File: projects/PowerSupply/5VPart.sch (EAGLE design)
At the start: 26 parts, among them IC1 LM2596T, IC2 LM2596T, X1 IN, X2 OUT

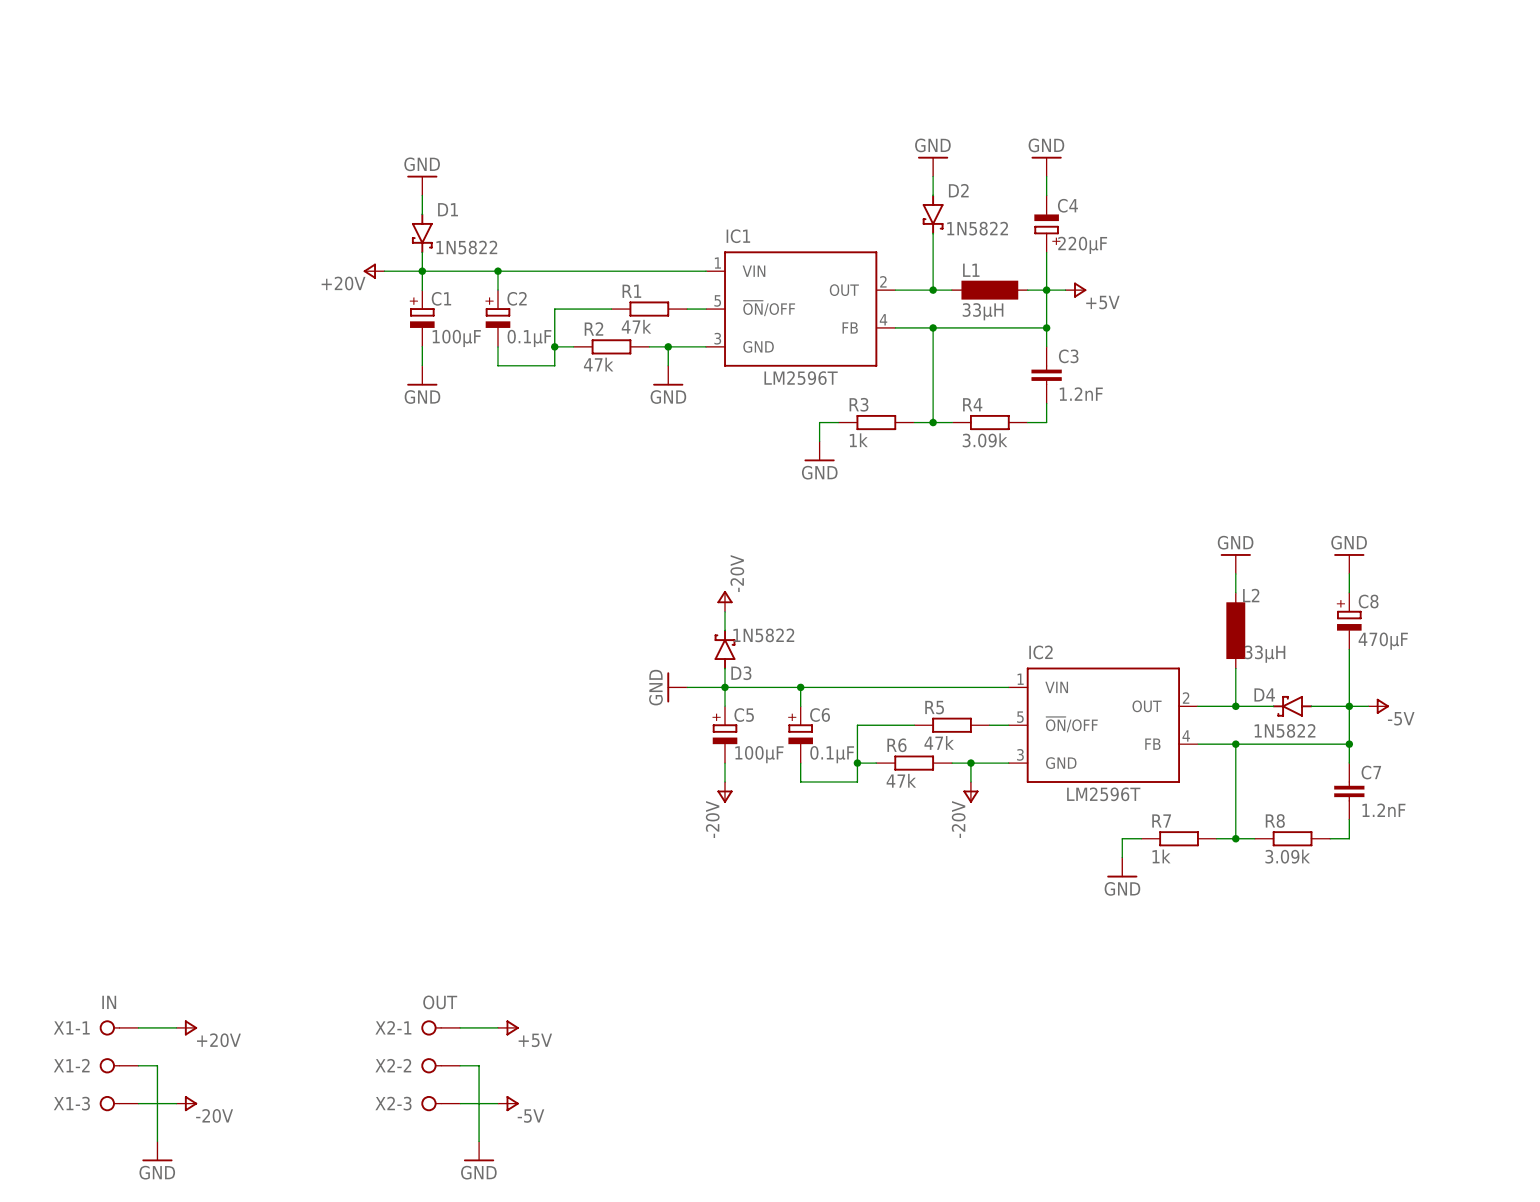
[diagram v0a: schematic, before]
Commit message: feat: 5 volt part modified
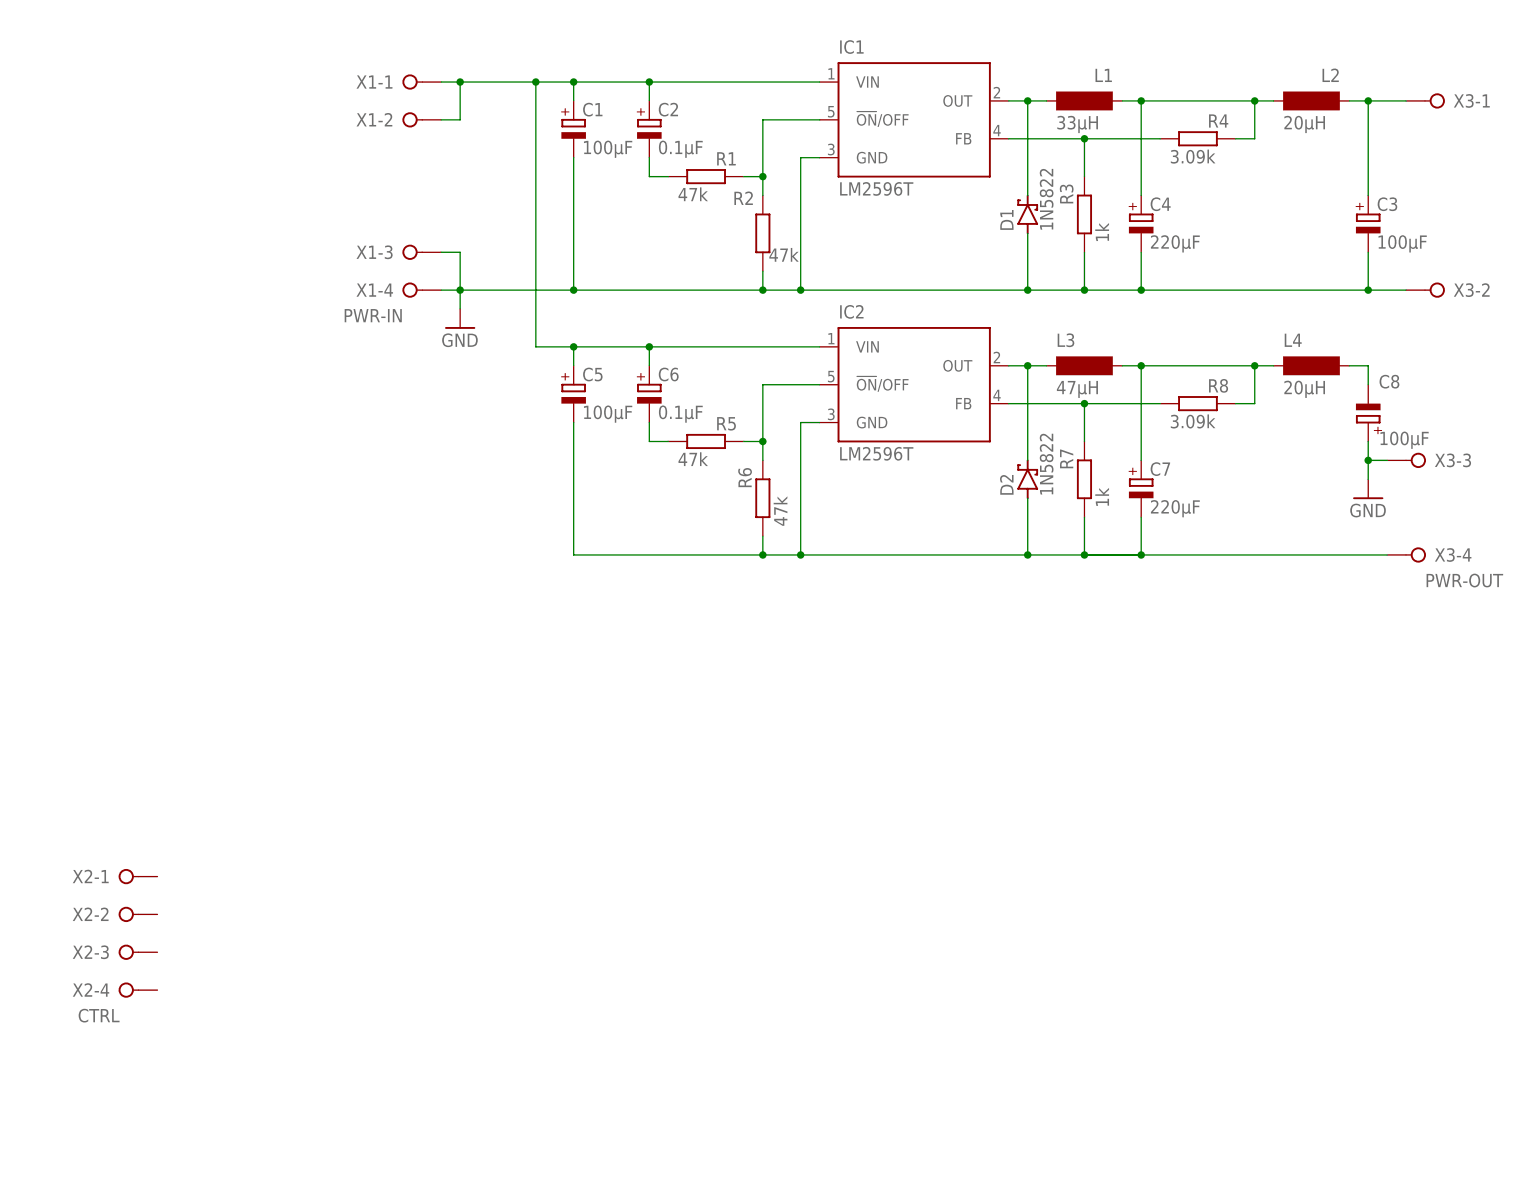
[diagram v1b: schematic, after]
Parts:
- removed D3, D4: 1N5822, diode:SCHOTTKY-DIODEC4111-15
- added L3: 47µH, bb84:IND-120-470K
- added L4: 20µH, bb84:B82111B0000C020
- added X3: PWR-OUT, con-wago-508:W237-04P
- C1, C5: device rcl:CPOL-EUE2.5-6 -> rcl:CPOL-EUE2.5-5
- C2, C6: device rcl:CPOL-EUE1.8-4 -> rcl:CPOL-EUE2-4
- C3: value 1.2nF -> 100µF; device rcl:C-EU050-024X044 -> rcl:CPOL-EUE2.5-5
- C7: value 1.2nF -> 220µF; device rcl:C-EU050-024X044 -> rcl:CPOL-EUE3.5-8
- C8: value 470µF -> 100µF; device rcl:CPOL-EUE3.5-8 -> rcl:CPOL-EUE2.5-5
- D1, D2: device diode:SCHOTTKY-DIODEC4111-15 -> diode:1N5908
- L2: value 33µH -> 20µH; device bb84:IND-120-330K -> bb84:B82111B0000C020
- X1: value IN -> PWR-IN; device con-wago-508:W237-03P -> con-wago-508:W237-04P
- X2: value OUT -> CTRL; device con-wago-508:W237-03P -> con-wago-508:W237-04P
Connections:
- removed net +20V: C1.+, C2.+, D1.C, IC1.VIN, X1-1.KL
- removed net +5V: C3.1, C4.+, IC1.FB, L1.2, R3.2, R4.1, X2-1.KL
- removed net -20V: C5.-, D3.C, IC2.GND, R6.2, X1-3.KL
- removed net -5V: C7.1, C8.-, D4.A, IC2.FB, R7.2, R8.1, X2-3.KL
- removed net N$3: D2.C, IC1.OUT, L1.1
- new net N$10: IC2.!ON!/OFF, R5.2, R6.2
- new net N$11: C5.-, C7.-, D2.A, IC2.GND, R6.1, R7.1, X3-4.KL
- new net N$12: D2.C, IC2.OUT, L3.1
- new net N$13: C7.+, L3.2, L4.1, R8.2
- new net N$14: IC2.FB, R7.2, R8.1
- new net N$15: C8.-, L4.2
- new net N$9: C6.-, R5.1
- net GND: now also C3.-, R2.1, X1-3.KL, X1-4.KL, X3-2.KL, X3-3.KL; no longer C5.+, C6.+, D2.A, D3.A, IC2.VIN, L2.2, R2.2, R7.1, X1-2.KL, X2-2.KL
- net N$1: now also C1.+, C2.+, C5.+, C6.+, IC1.VIN, IC2.VIN, X1-1.KL, X1-2.KL; no longer C3.2, R4.2
- net N$2: now also IC1.!ON!/OFF, R1.2, R2.2; no longer D4.C, IC2.OUT, L2.1
- net N$4: now also D1.C, IC1.OUT, L1.1; no longer IC1.!ON!/OFF, R1.2
- net N$5: now also IC1.FB, R3.2, R4.1; no longer C7.2, R8.2
- net N$6: now also C4.+, L1.2, L2.1, R4.2; no longer C2.-, R1.1, R2.1
- net N$7: now also C3.+, L2.2, X3-1.KL; no longer IC2.!ON!/OFF, R5.2
- net N$8: now also C2.-, R1.1; no longer C6.-, R5.1, R6.1
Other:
- moved on the sheet: C1, C2, C4, C5, C6, C8, IC1, IC2, L1, L2, R1, R2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

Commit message: feat: 5 volt part modified
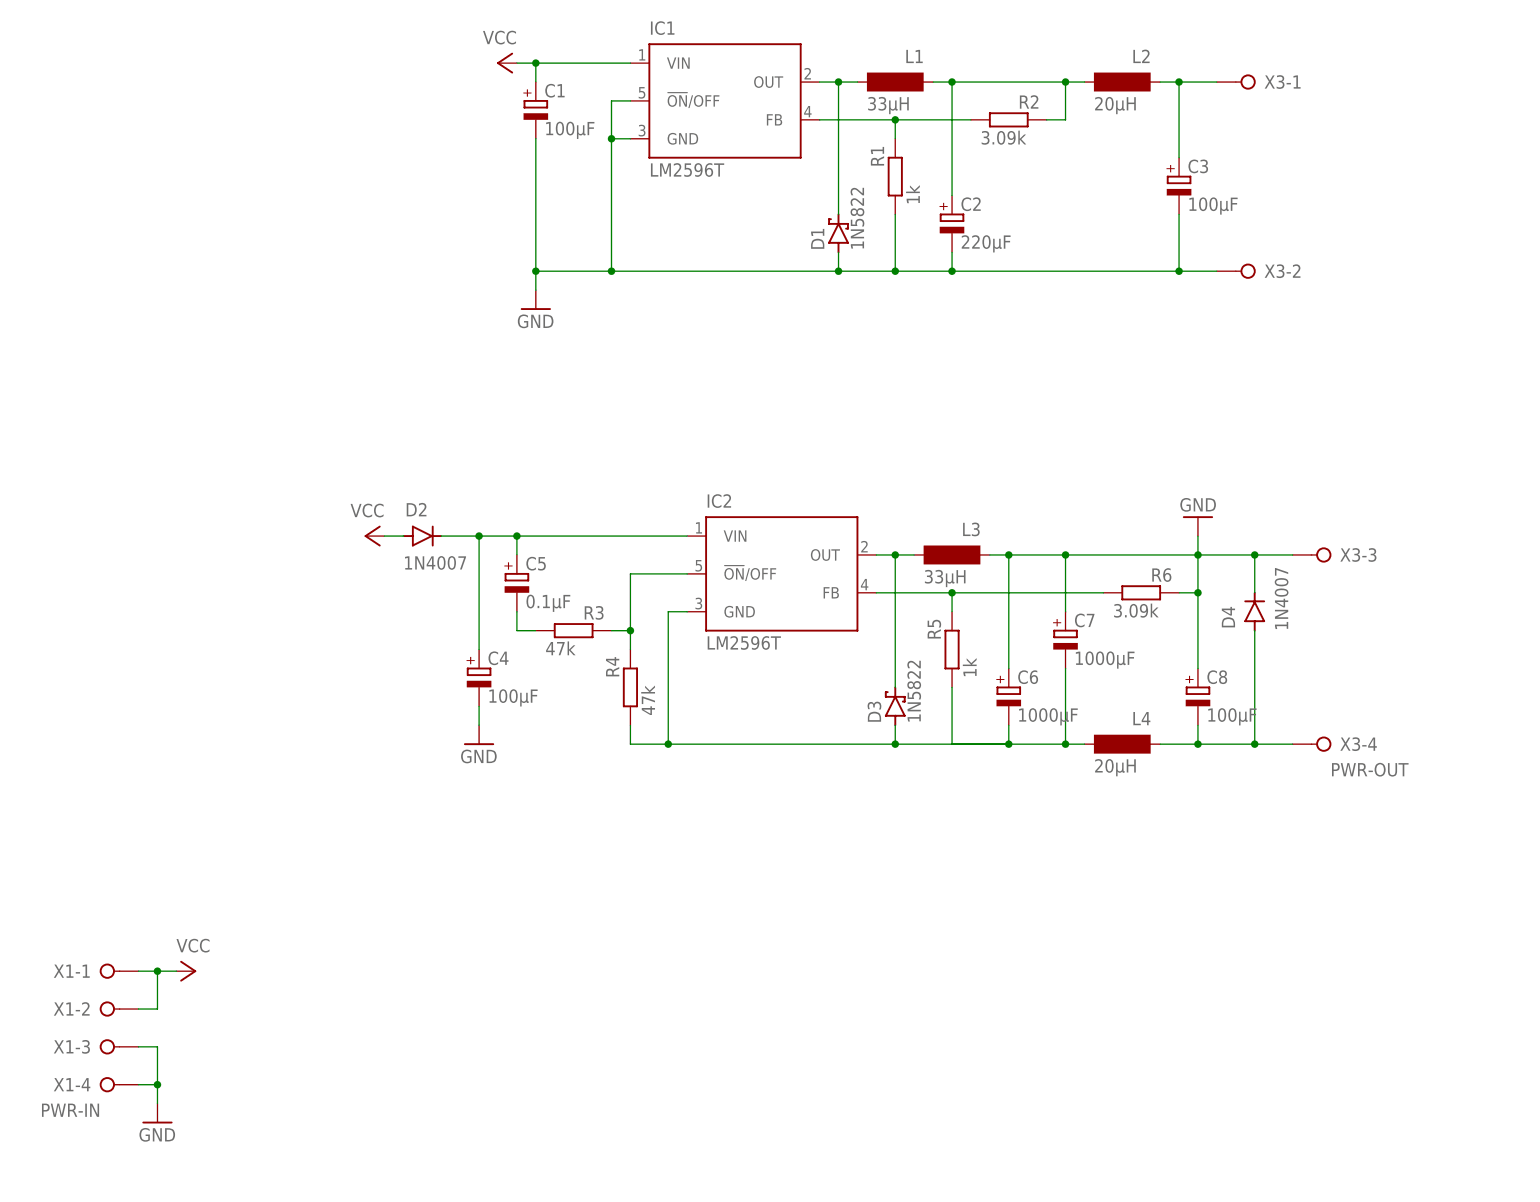
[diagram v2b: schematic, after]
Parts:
- removed R7: 1k, rcl:R-EU_0207/10
- removed R8: 3.09k, rcl:R-EU_0207/10
- removed X2: CTRL, con-wago-508:W237-04P
- added D3: 1N5822, diode:1N5908
- added D4: 1N4007, Diodes:1N4007
- C1, C3, C8: device rcl:CPOL-EUE2.5-5 -> rcl:CPOL-EUE2.5-6
- C2: value 0.1µF -> 220µF; device rcl:CPOL-EUE2-4 -> rcl:CPOL-EUE2.5-6
- C4: value 220µF -> 100µF; device rcl:CPOL-EUE3.5-8 -> rcl:CPOL-EUE2.5-6
- C5: value 100µF -> 0.1µF; device rcl:CPOL-EUE2.5-5 -> rcl:CPOL-EUE2-4
- C6: value 0.1µF -> 1000µF; device rcl:CPOL-EUE2-4 -> rcl:CPOL-EUE5-10.5
- C7: value 220µF -> 1000µF; device rcl:CPOL-EUE3.5-8 -> rcl:CPOL-EUE5-10.5
- D2: value 1N5822 -> 1N4007; device diode:1N5908 -> Diodes:1N4007
- L3: value 47µH -> 33µH
- R1, R5: value 47k -> 1k
- R2, R6: value 47k -> 3.09k
- R3: value 1k -> 47k
- R4: value 3.09k -> 47k
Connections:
- removed net N$13: C7.+, L3.2, L4.1, R8.2
- removed net N$15: C8.-, L4.2
- removed net N$2: IC1.!ON!/OFF, R1.2, R2.2
- removed net N$8: C2.-, R1.1
- new net N$3: C8.-, D4.A, L4.2, X3-4.KL
- new net VCC: C1.+, D2.A, IC1.VIN, X1-1.KL, X1-2.KL
- net GND: now also C2.-, C6.+, C7.+, D4.C, IC1.!ON!/OFF, L3.2, R1.1, R6.2; no longer R2.1, R3.1
- net N$1: now also C4.+, D2.C; no longer C1.+, C2.+, C6.+, IC1.VIN, X1-1.KL, X1-2.KL
- net N$10: now also R3.2, R4.2; no longer R5.2, R6.2
- net N$11: now also C6.-, D3.A, L4.1, R4.1, R5.1; no longer C5.-, D2.A, R6.1, R7.1, X3-4.KL
- net N$12: now also D3.C; no longer D2.C
- net N$14: now also R5.2, R6.1; no longer R7.2, R8.1
- net N$5: now also R1.2, R2.1; no longer R3.2, R4.1
- net N$6: now also C2.+, R2.2; no longer C4.+, R4.2
- net N$9: now also C5.-, R3.1; no longer C6.-, R5.1
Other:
- moved on the sheet: C1, C2, C3, C4, C5, C6, C7, C8, D1, IC1, IC2, L1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

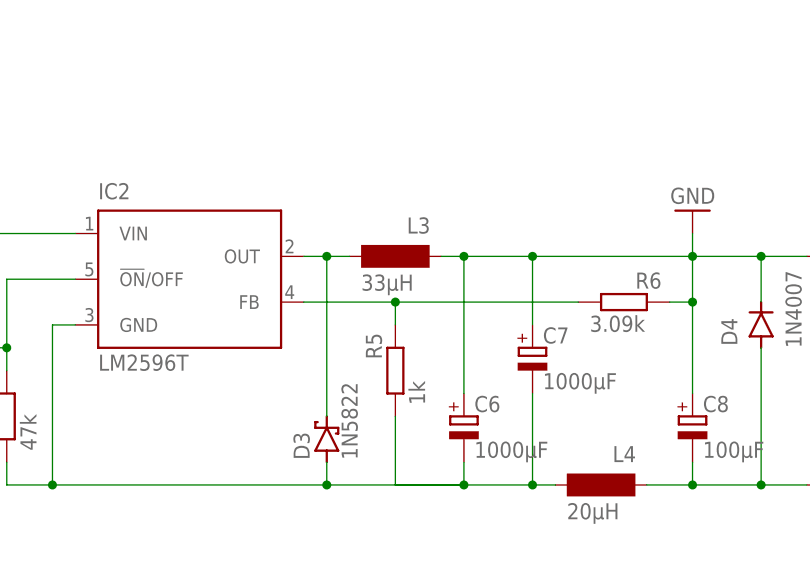
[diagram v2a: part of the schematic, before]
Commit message: feat: 5 volt part modified
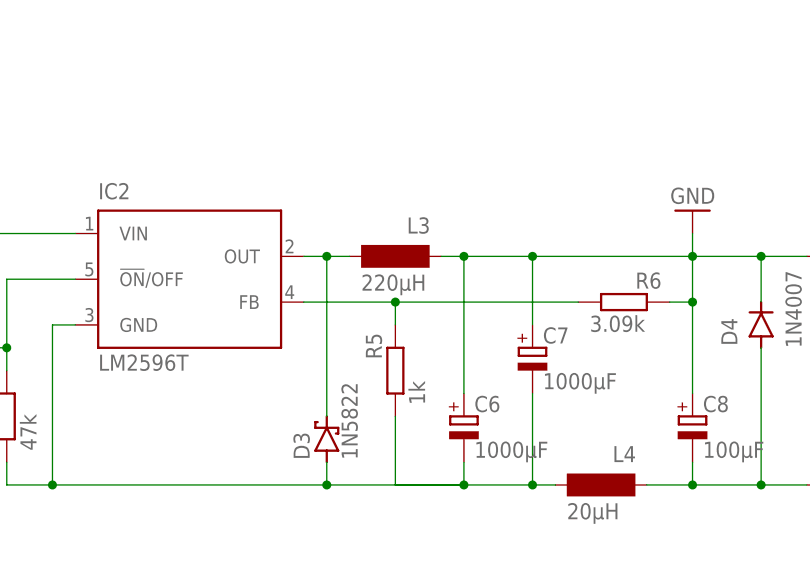
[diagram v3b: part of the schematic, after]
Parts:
- L3: value 33µH -> 220µH; device bb84:IND-120-470K -> bb84:11PHC-221K-50
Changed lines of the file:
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@@
 <part name="R6" library="rcl" library_urn="urn:adsk.eagle:library:334" deviceset="R-EU_" device="0207/10" package3d_urn="urn:adsk.eagle:package:23491/2" value="3.09k"/>
 <part name="C6" library="rcl" library_urn="urn:adsk.eagle:library:334" deviceset="CPOL-EU" device="E5-10.5" package3d_urn="urn:adsk.eagle:package:23372/2" value="1000µF"/>
-<part name="L3" library="bb84" deviceset="IND-120-470K" device="" value="33µH"/>
+<part name="L3" library="bb84" deviceset="11PHC-221K-50" device="" value="220µH"/>
 <part name="L4" library="bb84" deviceset="B82111B0000C020" device="" value="20µH"/>
 <part name="C8" library="rcl" library_urn="urn:adsk.eagle:library:334" deviceset="CPOL-EU" device="E2.5-6" package3d_urn="urn:adsk.eagle:package:23349/1" value="100µF"/>
